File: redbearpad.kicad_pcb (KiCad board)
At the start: 2 copper layers, 96 x 64 mm, 15 parts, among them J1 PinSocket_1x14_P2.54mm_Vertic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, J2 PinSocket_1x14_P2.54mm_Vertic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, J3 PinSocket_1x04_P2.54mm_Vertic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, SW1 SW_Redragon_LowProfile_PCB_1.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, SW2 SW_Redragon_LowProfile_PCB_1.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, SW3 SW_Redragon_LowProfile_PCB_1.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, SW4 SW_Redragon_LowProfile_PCB_1.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, SW5 SW_Redragon_LowProfile_PCB_1.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, SW6 SW_Redragon_LowProfile_PCB_1.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, SW7 SW_Redragon_LowProfile_PCB_1.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, SW8 SW_Redragon_LowProfile_PCB_1.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

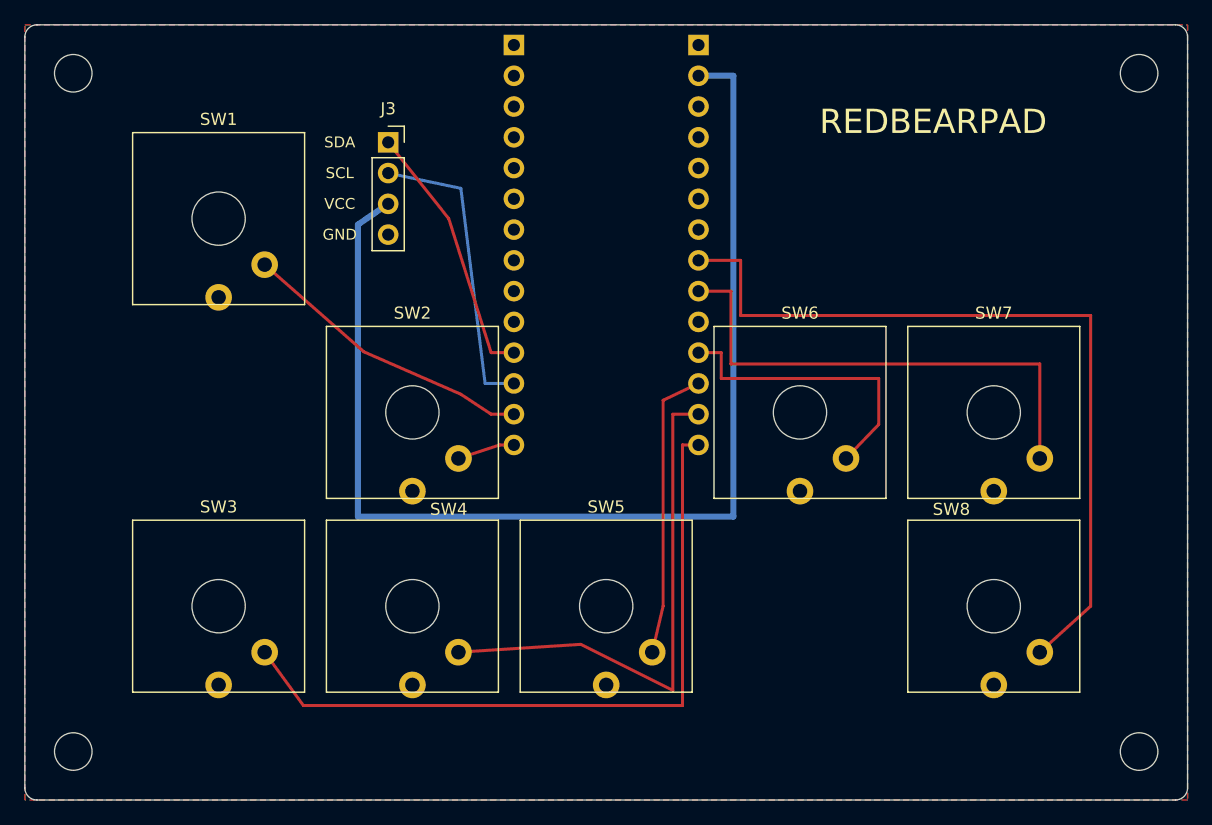
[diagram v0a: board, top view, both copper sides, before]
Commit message: feat(pcb-v2): placement de 12 footprints, OLED fuera (sin pistas aun)
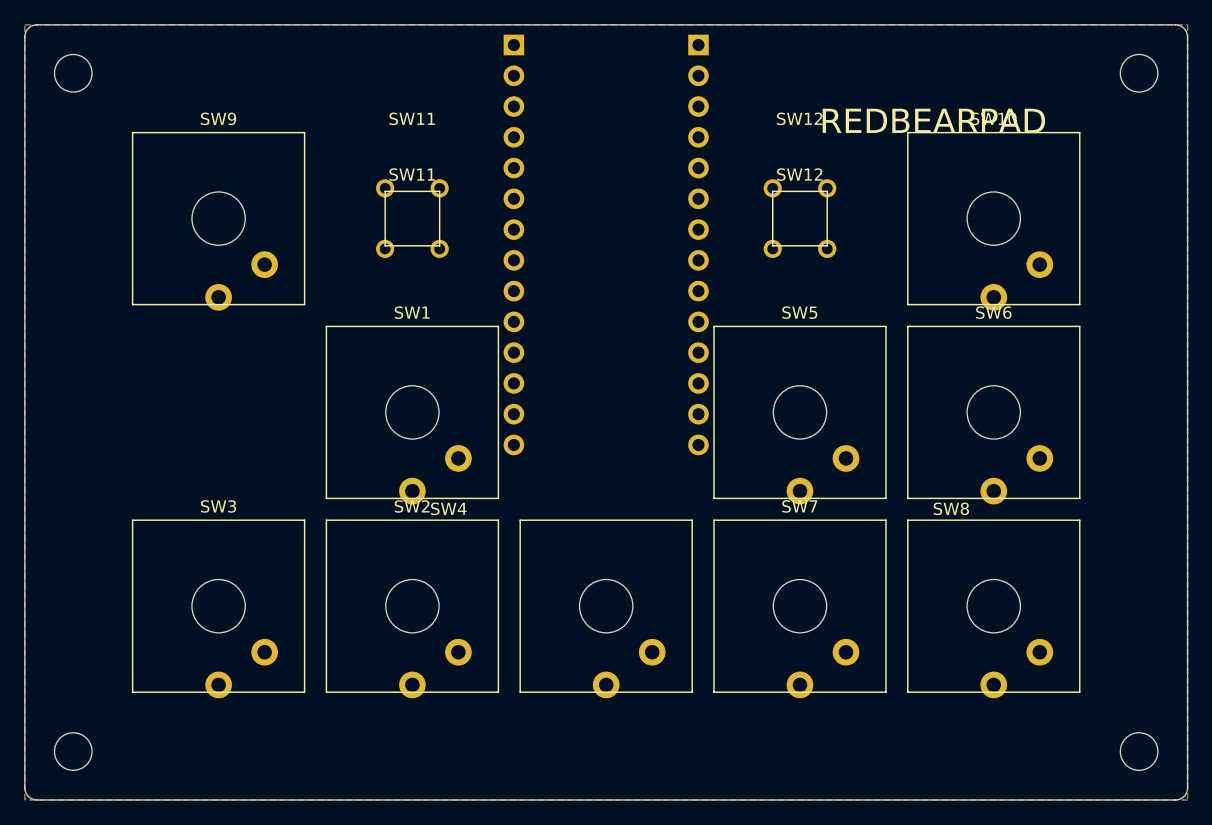
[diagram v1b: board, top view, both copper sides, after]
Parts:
- removed J3: PinSocket_1x04_P2.54mm_Vertical, PinSocket_1x04_P2.54mm_Vertical
- added SW10: SW_Redragon_LowProfile_PCB_1.00u, SW_Redragon_LowProfile_PCB_1.00u, F.Cu at (80.0, 16.0)
- added SW11: SW_Tact_CAX, SW_Tact_CAX_4.5x4.5, F.Cu at (32.0, 16.0)
- added SW12: SW_Tact_CAX, SW_Tact_CAX_4.5x4.5, F.Cu at (64.0, 16.0)
- added SW9: SW_Redragon_LowProfile_PCB_1.00u, SW_Redragon_LowProfile_PCB_1.00u, F.Cu at (16.0, 16.0)
- moved SW1 22.6 mm to (32.0, 32.0)
- moved SW5 22.6 mm to (64.0, 32.0)
- moved SW7 22.6 mm to (64.0, 48.0)
- moved SW2 16.0 mm to (32.0, 48.0)
- moved SW4 16.0 mm to (48.0, 48.0)
- moved SW6 16.0 mm to (80.0, 32.0)
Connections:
- J1 pad 10: (no net) -> SW2
- J1 pad 11: SDA -> SW3
- J1 pad 12: SCL -> SW1
- J1 pad 13: SW1 -> SW11
- J1 pad 14: SW2 -> SW9
- J1 pad 9: (no net) -> SW4
- J2 pad 13: SW4 -> SW12
- J2 pad 14: SW3 -> SW10
- J2 pad 2: +3V3 -> (no net)
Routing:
- net +3V3: track 97.4 -> 0.00 mm
- net SW8: track 66.6 -> 0.00 mm
- net SW3: track 59.6 -> 0.00 mm
- net SW4: track 43.5 -> 0.00 mm
- net SW7: track 42.0 -> 0.00 mm
- net SCL: track 24.7 -> 0.00 mm
- net SW6: track 24.7 -> 0.00 mm
- net SW1: track 24.5 -> 0.00 mm
- net SW5: track 24.1 -> 0.00 mm
- net SDA: track 21.5 -> 0.00 mm
- net SW2: track 4.76 -> 0.00 mm
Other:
- board text added: "SW10"
- board text added: "SW11"
- board text added: "SW12"
- board text added: "SW9"
- board text removed: "GND"
- board text removed: "SCL"
- board text removed: "SDA"
- board text removed: "VCC"

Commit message: feat(pcb-v2): ruteo completo de 12 nets (Freerouting 11 + SW7 con via a mano), DRC de cobre limpio
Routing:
- net SW8: track 0.00 -> 44.0 mm
- net SW10: track 0.00 -> 40.8 mm
- net SW7: track 0.00 -> 40.7 mm, vias 0 -> 1
- net SW3: track 0.00 -> 37.3 mm
- net SW4: track 0.00 -> 34.5 mm
- net SW6: track 0.00 -> 31.8 mm
- net SW2: track 0.00 -> 30.6 mm
- net SW9: track 0.00 -> 26.7 mm
- net SW12: track 0.00 -> 23.3 mm
- net SW11: track 0.00 -> 23.1 mm
- net SW5: track 0.00 -> 14.7 mm
- net SW1: track 0.00 -> 8.09 mm

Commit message: feat(pcb-v2): serigrafia limpia (refdes ocultos, etiquetas duplicadas fuera); quedan 8 silk-over-pad cosmeticas del tact
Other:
- board text removed: "SW1"
- board text removed: "SW10"
- board text removed: "SW11"
- board text removed: "SW12"
- board text removed: "SW2"
- board text removed: "SW3"
- board text removed: "SW4"
- board text removed: "SW5"
- board text removed: "SW6"
- board text removed: "SW7"
- board text removed: "SW8"
- board text removed: "SW9"
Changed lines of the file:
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@@
 		(property "Reference" "SW4"
 			(at 0 4 0)
-			(layer "B.SilkS")
+			(layer "F.SilkS")
+			(hide yes)
 			(effects
 				(font
@@
 			(at 0 8 0)
 			(layer "F.Fab")
+			(hide yes)
 			(effects
 				(font
@@
 		(property "Reference" "SW8"
 			(at 0 4 0)
-			(layer "B.SilkS")
+			(layer "F.SilkS")
+			(hide yes)
 			(effects
 				(font
@@
 			(at 0 8 0)
 			(layer "F.Fab")
+			(hide yes)
 			(effects
 				(font
@@
 		(property "Reference" "SW10"
 			(at 0 4 0)
-			(layer "B.SilkS")
+			(layer "F.SilkS")
+			(hide yes)
 			(effects
 				(font
@@
 			(at 0 8 0)
 			(layer "F.Fab")
+			(hide yes)
 			(effects
 				(font
@@
 		(property "Reference" "SW1"
 			(at 0 4 0)
-			(layer "B.SilkS")
+			(layer "F.SilkS")
+			(hide yes)
 			(effects
 				(font
@@
 			(at 0 8 0)
 			(layer "F.Fab")
+			(hide yes)
 			(effects
 				(font
@@
 		(property "Reference" "SW2"
 			(at 0 4 0)
-			(layer "B.SilkS")
+			(layer "F.SilkS")
+			(hide yes)
 			(effects
 				(font
@@
 			(at 0 8 0)
 			(layer "F.Fab")
+			(hide yes)
 			(effects
 				(font
@@
 		(property "Reference" "SW9"
 			(at 0 4 0)
-			(layer "B.SilkS")
+			(layer "F.SilkS")
+			(hide yes)
 			(effects
 				(font
@@
 			(at 0 8 0)
 			(layer "F.Fab")
+			(hide yes)
 			(effects
 				(font
@@
 		(property "Reference" "SW5"
 			(at 0 4 0)
-			(layer "B.SilkS")
+			(layer "F.SilkS")
+			(hide yes)
 			(effects
 				(font
@@
 			(at 0 8 0)
 			(layer "F.Fab")
+			(hide yes)
 			(effects
 				(font
@@
 		(property "Reference" "SW6"
 			(at 0 4 0)
-			(layer "B.SilkS")
+			(layer "F.SilkS")
+			(hide yes)
 			(effects
 				(font
@@
 			(at 0 8 0)
 			(layer "F.Fab")
+			(hide yes)
 			(effects
 				(font
@@
 			(at 0 -3.6 0)
 			(layer "F.SilkS")
+			(hide yes)
 			(effects
 				(font
@@
 			(at 0 3.6 0)
 			(layer "F.Fab")
+			(hide yes)
 			(effects
 				(font
@@
 		(property "Reference" "SW3"
 			(at 0 4 0)
-			(layer "B.SilkS")
+			(layer "F.SilkS")
+			(hide yes)
 			(effects
 				(font
@@
 			(at 0 8 0)
 			(layer "F.Fab")
+			(hide yes)
 			(effects
 				(font
@@
 		(property "Reference" "SW7"
 			(at 0 4 0)
-			(layer "B.SilkS")
+			(layer "F.SilkS")
+			(hide yes)
 			(effects
 				(font
@@
 			(at 0 8 0)
 			(layer "F.Fab")
+			(hide yes)
 			(effects
 				(font
@@
 			(at 0 -3.6 0)
 			(layer "F.SilkS")
+			(hide yes)
 			(effects
 				(font
@@
 			(at 0 3.6 0)
 			(layer "F.Fab")
+			(hide yes)
 			(effects
 				(font
@@
 		(property "Reference" "J2"
 			(at 0 2.77 0)
-			(layer "B.SilkS")
+			(layer "F.SilkS")
+			(hide yes)
 			(effects
 				(font
@@
 			(at 0 -35.79 0)
 			(layer "B.Fab")
+			(hide yes)
 			(effects
 				(font
@@
 		(property "Reference" "J1"
 			(at 0 2.77 0)
-			(layer "B.SilkS")
+			(layer "F.SilkS")
+			(hide yes)
 			(effects
 				(font
@@
 			(at 0 -35.79 0)
 			(layer "B.Fab")
+			(hide yes)
 			(effects
 				(font
@@
 		(layer "Edge.Cuts")
 	)
-	(gr_text "SW7"
-		(at 64 39.8 0)
-		(layer "F.SilkS")
-		(effects
-			(font
-				(size 1 1)
-				(thickness 0.2)
-			)
-		)
-	)
-	(gr_text "SW9"
-		(at 16 7.8 0)
-		(layer "F.SilkS")
-		(effects
-			(font
-				(size 1 1)
-				(thickness 0.2)
-			)
-		)
-	)
 	(gr_text "REDBEARPAD"
-		(at 75 8 0)
-		(layer "F.SilkS")
-		(effects
-			(font
-				(size 2 2)
-				(thickness 0.2)
-			)
-		)
-	)
-	(gr_text "SW6"
-		(at 80 23.8 0)
-		(layer "F.SilkS")
-		(effects
-			(font
-				(size 1 1)
-				(thickness 0.2)
-			)
-		)
-	)
-	(gr_text "SW10"
-		(at 80 7.8 0)
-		(layer "F.SilkS")
-		(effects
-			(font
-				(size 1 1)
-				(thickness 0.2)
-			)
-		)
-	)
-	(gr_text "SW1"
-		(at 32 23.8 0)
-		(layer "F.SilkS")
-		(effects
-			(font
-				(size 1 1)
-				(thickness 0.2)
-			)
-		)
-	)
-	(gr_text "SW8"
-		(at 76.5 40 0)
-		(layer "F.SilkS")
-		(effects
-			(font
-				(size 1 1)
-				(thickness 0.2)
-			)
-		)
-	)
-	(gr_text "SW2"
-		(at 32 39.8 0)
-		(layer "F.SilkS")
-		(effects
-			(font
-				(size 1 1)
-				(thickness 0.2)
-			)
-		)
-	)
-	(gr_text "SW4"
-		(at 35 40 0)
-		(layer "F.SilkS")
-		(effects
-			(font
-				(size 1 1)
-				(thickness 0.2)
-			)
-		)
-	)
-	(gr_text "SW5"
-		(at 64 23.8 0)
-		(layer "F.SilkS")
-		(effects
-			(font
-				(size 1 1)
-				(thickness 0.2)
-			)
-		)
-	)
-	(gr_text "SW12"
-		(at 64 7.8 0)
-		(layer "F.SilkS")
-		(effects
-			(font
-				(size 1 1)
-				(thickness 0.2)
-			)
-		)
-	)
-	(gr_text "SW3"
-		(at 16 39.8 0)
-		(layer "F.SilkS")
-		(effects
-			(font
-				(size 1 1)
-				(thickness 0.2)
-			)
-		)
-	)
-	(gr_text "SW11"
-		(at 32 7.8 0)
+		(at 48 60 0)
 		(layer "F.SilkS")
 		(effects
 			(font
-				(size 1 1)
+				(size 1.6 1.6)
 				(thickness 0.2)
 			)
